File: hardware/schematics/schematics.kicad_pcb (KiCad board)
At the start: 2 copper layers, 25 parts, among them J1 Jack-DC, J2 Conn_01x20, J3 Conn_01x20, Q1 Q_NMOS_DGS, U1 ESP32-DevKitC, U2 L7805, U3 MAX6921AUI+

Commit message: Main PCB completed
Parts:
- added REF**: TestPoint_Plated_Hole_D2.0mm, TestPoint:TestPoint_Plated_Hole_D2.0mm, F.Cu at (130.8, 128.3)
- added REF**: TestPoint_Plated_Hole_D2.0mm, TestPoint:TestPoint_Plated_Hole_D2.0mm, F.Cu at (156.2, 125.7)
- added REF**: TestPoint_Plated_Hole_D2.0mm, TestPoint:TestPoint_Plated_Hole_D2.0mm, F.Cu at (92.7, 121.9)
- added REF**: MountingHole_3.2mm_M3_Pad, MountingHole:MountingHole_3.2mm_M3_Pad, F.Cu at (163.8, 137.2)
- added REF**: MountingHole_3.2mm_M3_Pad, MountingHole:MountingHole_3.2mm_M3_Pad, F.Cu at (74.9, 137.2)
- added REF**: MountingHole_3.2mm_M3_Pad, MountingHole:MountingHole_3.2mm_M3_Pad, F.Cu at (74.9, 83.8)
- added REF**: MountingHole_3.2mm_M3_Pad, MountingHole:MountingHole_3.2mm_M3_Pad, F.Cu at (163.8, 83.8)
- F1: footprint Capacitor_THT:C_Disc_D7.5mm_W4.4mm_P5.00mm -> Fuse:Fuse_Littelfuse_395Series
- J2: footprint Connector_PinHeader_2.54mm:PinHeader_2x10_P2.54mm_Vertical -> Connector_PinSocket_2.54mm:PinSocket_2x10_P2.54mm_Horizontal
- J3: footprint Connector_PinHeader_2.54mm:PinHeader_2x10_P2.54mm_Vertical -> Connector_PinSocket_2.54mm:PinSocket_2x10_P2.54mm_Vertical
- U2: footprint Package_TO_SOT_THT:TO-220-3_Vertical -> Package_TO_SOT_THT:TO-220-3_Horizontal_TabDown
- U3: footprint callisto:MAX6921AUI+ -> Package_SO:TSSOP-28_4.4x9.7mm_P0.65mm
- moved J1 149.4 mm to (152.4, 134.2), turned to 90 degrees
- moved L1 97.8 mm to (105.4, 138.4), turned to 90 degrees
- moved Q1 95.2 mm to (109.2, 128.3), turned to 180 degrees
- moved F1 72.0 mm to (144.8, 133.3), turned to 270 degrees
- moved C2 70.2 mm to (138.4, 123.2), turned to 90 degrees
- moved U2 69.5 mm to (133.3, 138.4), turned to 90 degrees
- moved C1 69.0 mm to (144.8, 123.2), turned to 90 degrees
- moved U1 63.3 mm to (143.5, 102.9), turned to 90 degrees
- moved J2 62.0 mm to (105.4, 83.8), turned to 270 degrees
- moved C4 61.6 mm to (137.2, 135.9)
- moved D4 59.9 mm to (82.5, 128.3), turned to 270 degrees
- moved D2 55.7 mm to (144.8, 128.3)
- moved D3 53.9 mm to (87.6, 128.3)
- moved D1 52.9 mm to (165.1, 120.7), turned to 180 degrees
- moved C6 49.9 mm to (88.9, 133.4), turned to 270 degrees
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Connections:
- J1 pad 3: (no net) -> GND
- J2 pad 10: /dig_3 -> /O_4
- J2 pad 11: /dig_2 -> /O_19
- J2 pad 12: /dig_1 -> /O_3
- J2 pad 13: /seg_h -> /O_18
- J2 pad 14: /seg_g -> /O_2
- J2 pad 15: /seg_f -> /O_17
- J2 pad 16: /seg_e -> /O_1
- J2 pad 17: /seg_d -> /O_16
- J2 pad 18: /seg_c -> /O_0
- J2 pad 19: /seg_b -> GND
- J2 pad 2: GND -> /O_8
- J2 pad 20: /seg_a -> GND
- J2 pad 3: /fil_v -> /O_13
- J2 pad 4: /dig_9 -> /O_7
- J2 pad 5: /dig_8 -> /O_12
- J2 pad 6: /dig_7 -> /O_6
- J2 pad 7: /dig_6 -> /O_11
- J2 pad 8: /dig_5 -> /O_5
- J2 pad 9: /dig_4 -> /O_10
- R3 pad 1: VCC -> Net-(J2-Pad1)
- R3 pad 2: /fil_v -> VCC
- U1 pad J2_11: /BLANK -> Net-(U1-PadJ2_11)
- U1 pad J2_3: Net-(U1-PadJ2_3) -> /BRIGHTNESS
- U1 pad J2_7: /BRIGHTNESS -> /PWM
- U1 pad J3_12: /PWM -> Net-(U1-PadJ3_12)
- U1 pad J3_6: Net-(U1-PadJ3_6) -> /BLANK
- U3 pad 1: /seg_e -> /O_4
- U3 pad 10: Net-(U3-Pad10) -> /O_19
- U3 pad 11: Net-(U3-Pad11) -> /O_18
- U3 pad 12: Net-(U3-Pad12) -> /O_17
- U3 pad 13: /dig_9 -> /O_16
- U3 pad 14: /dig_8 -> Net-(U3-Pad14)
- U3 pad 15: /dig_7 -> Net-(U3-Pad15)
- U3 pad 16: /dig_6 -> /O_13
- U3 pad 17: /dig_5 -> /O_12
- U3 pad 18: /dig_4 -> /O_11
- U3 pad 19: /dig_3 -> /O_10
- U3 pad 2: /seg_d -> /O_3
- U3 pad 24: /dig_2 -> Net-(U3-Pad24)
- U3 pad 25: /dig_1 -> /O_8
- U3 pad 26: /seg_h -> /O_7
- U3 pad 27: /seg_g -> /O_6
- U3 pad 28: /seg_f -> /O_5
- U3 pad 3: /seg_c -> /O_2
- U3 pad 4: /seg_b -> /O_1
- U3 pad 5: /seg_a -> /O_0
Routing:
- net VCC: track 0.00 -> 110.9 mm, vias 0 -> 2
- net +9V: track 0.00 -> 87.2 mm
- net /DIN: track 0.00 -> 63.8 mm
- net /LOAD: track 0.00 -> 61.9 mm, vias 0 -> 2
- net /CLK: track 0.00 -> 55.7 mm, vias 0 -> 2
- net /BLANK: track 0.00 -> 53.0 mm
- net VBB: track 0.00 -> 48.7 mm
- net /BRIGHTNESS: track 0.00 -> 40.0 mm, vias 0 -> 1
- net +3V3: track 0.00 -> 35.7 mm, vias 0 -> 1
- net /PWM: track 0.00 -> 30.9 mm
- net /O_13: track 0.00 -> 28.2 mm, vias 0 -> 1
- net /O_16: track 0.00 -> 28.2 mm, vias 0 -> 1
- net /O_12: track 0.00 -> 27.2 mm, vias 0 -> 1
- net /O_17: track 0.00 -> 27.2 mm, vias 0 -> 1
- net /O_11: track 0.00 -> 26.2 mm, vias 0 -> 1
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- added copper zone on B.Cu, net GND
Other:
- board outline added: 99.1 x 63.5 mm
- board text added: "9V"
- board text added: "VBB"
- board text added: "VCC"

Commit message: Tube PCB wired
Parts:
- removed the REF** at (163.8, 137.2)
- removed the REF** at (74.9, 137.2)
- removed the REF** at (74.9, 83.8)
- added REF**: MountingHole_3.2mm_M3_Pad, MountingHole:MountingHole_3.2mm_M3_Pad, F.Cu at (248.9, 148.0)
- added REF**: MountingHole_3.2mm_M3_Pad, MountingHole:MountingHole_3.2mm_M3_Pad, F.Cu at (160.0, 148.0)
- added REF**: MountingHole_3.2mm_M3_Pad, MountingHole:MountingHole_3.2mm_M3_Pad, F.Cu at (160.0, 94.6)
- J2: footprint Connector_PinSocket_2.54mm:PinSocket_2x10_P2.54mm_Horizontal -> Connector_PinSocket_2.54mm:PinSocket_2x10_P2.54mm_Vertical
- moved J3 146.4 mm to (60.3, 65.4), turned to 180 degrees
- moved DS1 122.6 mm to (93.3, 51.4), turned to 0 degrees
- moved REF** 85.8 mm to (177.8, 132.7)
- moved U3 85.8 mm to (179.1, 113.7)
- moved C1 85.8 mm to (229.9, 134.0)
- moved C2 85.8 mm to (223.5, 134.0)
- moved C3 85.8 mm to (222.2, 141.6)
- moved C4 85.8 mm to (222.2, 146.7)
- moved C5 85.8 mm to (236.2, 134.0)
- moved C6 85.8 mm to (174.0, 144.2)
- moved C7 85.8 mm to (180.3, 144.2)
- moved D1 85.8 mm to (250.2, 131.4)
- moved D2 85.8 mm to (229.9, 139.1)
- moved D3 85.8 mm to (172.7, 139.1)
- moved F1 85.8 mm to (229.9, 144.1)
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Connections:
- DS1 pad 1: GND -> /fil_g
- J1 pad 3: GND -> (no net)
- J2 pad 1: Net-(J2-Pad1) -> GND
- J2 pad 19: GND -> Net-(J2-Pad19)
- J3 pad 1: Net-(J3-Pad1) -> /dig_2
- J3 pad 10: /dig_3 -> /seg_h
- J3 pad 11: /dig_2 -> /dig_5
- J3 pad 12: /dig_1 -> /seg_a
- J3 pad 13: /seg_h -> /dig_3
- J3 pad 14: /seg_g -> /seg_f
- J3 pad 15: /seg_f -> /dig_1
- J3 pad 16: /seg_e -> /seg_b
- J3 pad 17: /seg_d -> /dig_9
- J3 pad 18: /seg_c -> /seg_g
- J3 pad 19: /seg_b -> Net-(J3-Pad19)
- J3 pad 2: GND -> /fil_g
- J3 pad 20: /seg_a -> /fil_v
- J3 pad 3: /fil_v -> /dig_4
- J3 pad 4: /dig_9 -> /seg_e
- J3 pad 5: /dig_8 -> /dig_6
- J3 pad 6: /dig_7 -> /seg_c
- J3 pad 7: /dig_6 -> /dig_7
- J3 pad 8: /dig_5 -> /seg_d
- J3 pad 9: /dig_4 -> /dig_8
- R3 pad 1: Net-(J2-Pad1) -> Net-(J2-Pad19)
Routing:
- net /seg_e: track 0.00 -> 40.0 mm
- net /seg_g: track 0.00 -> 39.5 mm
- net /seg_b: track 0.00 -> 38.0 mm
- net /seg_c: track 0.00 -> 36.8 mm
- net /seg_f: track 0.00 -> 36.8 mm
- net /seg_a: track 0.00 -> 35.1 mm
- net /seg_d: track 0.00 -> 34.7 mm
- net /dig_2: track 0.00 -> 34.1 mm
- net /fil_g: track 0.00 -> 33.0 mm
- net /seg_h: track 0.00 -> 33.0 mm
- net /dig_4: track 0.00 -> 32.0 mm
- net /dig_9: track 0.00 -> 32.0 mm
- net /fil_v: track 0.00 -> 30.9 mm
- net Net-(J2-Pad19): track 0.00 -> 30.5 mm
- net /dig_6: track 0.00 -> 30.4 mm
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
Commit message: Tube PCB created
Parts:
- moved J3 105.3 mm to (164.5, 81.3)
- moved DS1 92.7 mm to (184.8, 66.6)
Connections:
- J3 pad 19: Net-(J3-Pad19) -> (no net)
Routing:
- net /fil_v: track 30.9 -> 17.9 mm
- net /dig_9: track 32.0 -> 19.0 mm
- net /dig_1: track 29.9 -> 17.0 mm
- net /seg_h: track 33.0 -> 20.1 mm
- net /seg_d: track 34.7 -> 22.0 mm
- net /seg_c: track 36.8 -> 24.4 mm
- net /dig_4: track 32.0 -> 19.6 mm
- net /seg_e: track 40.0 -> 27.6 mm
- net /dig_6: track 30.4 -> 18.0 mm
- net /dig_8: track 28.7 -> 16.3 mm
- net /dig_7: track 29.3 -> 16.9 mm
- net /dig_5: track 28.6 -> 16.1 mm
- net /dig_3: track 28.9 -> 16.4 mm
- net /dig_2: track 34.1 -> 21.7 mm
- net /fil_g: track 33.0 -> 20.6 mm
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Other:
- board size 99.1 x 63.5 mm -> 99.2 x 96.4 mm

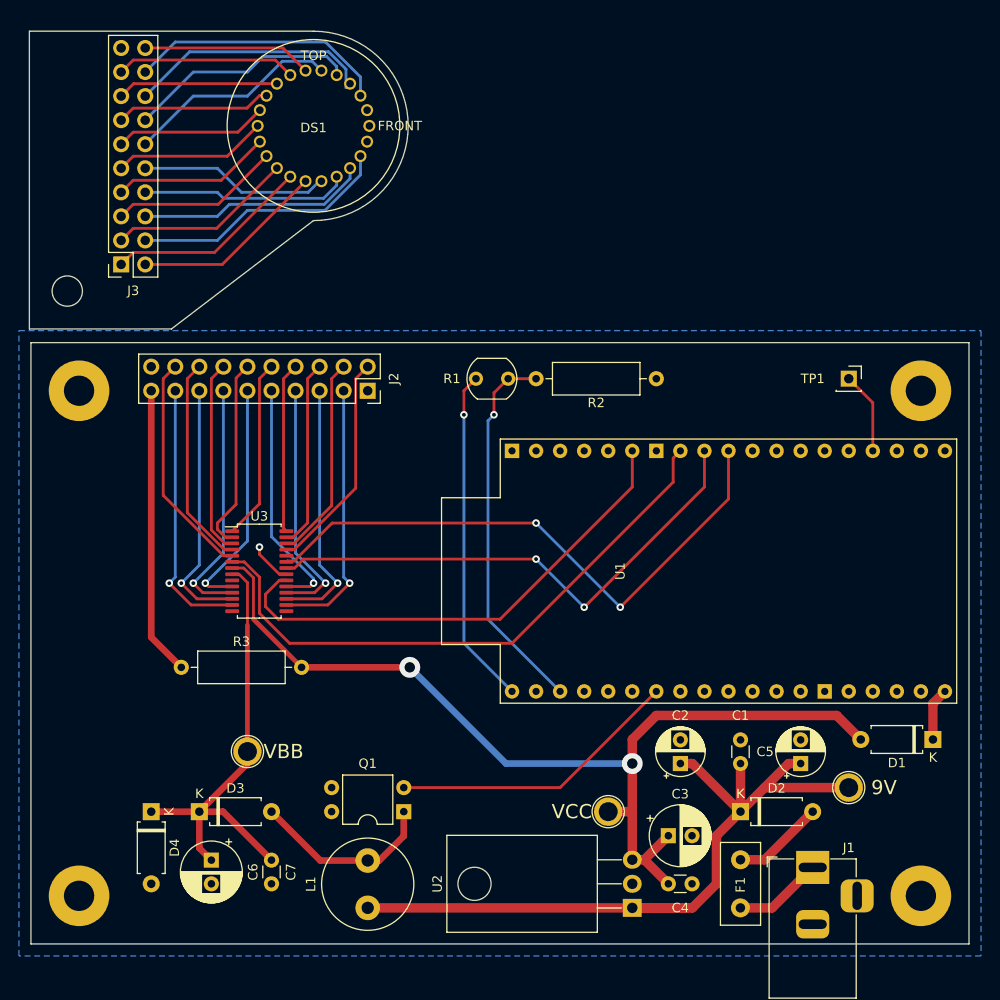
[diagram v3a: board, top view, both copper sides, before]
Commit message: Capacitor placements tweaked
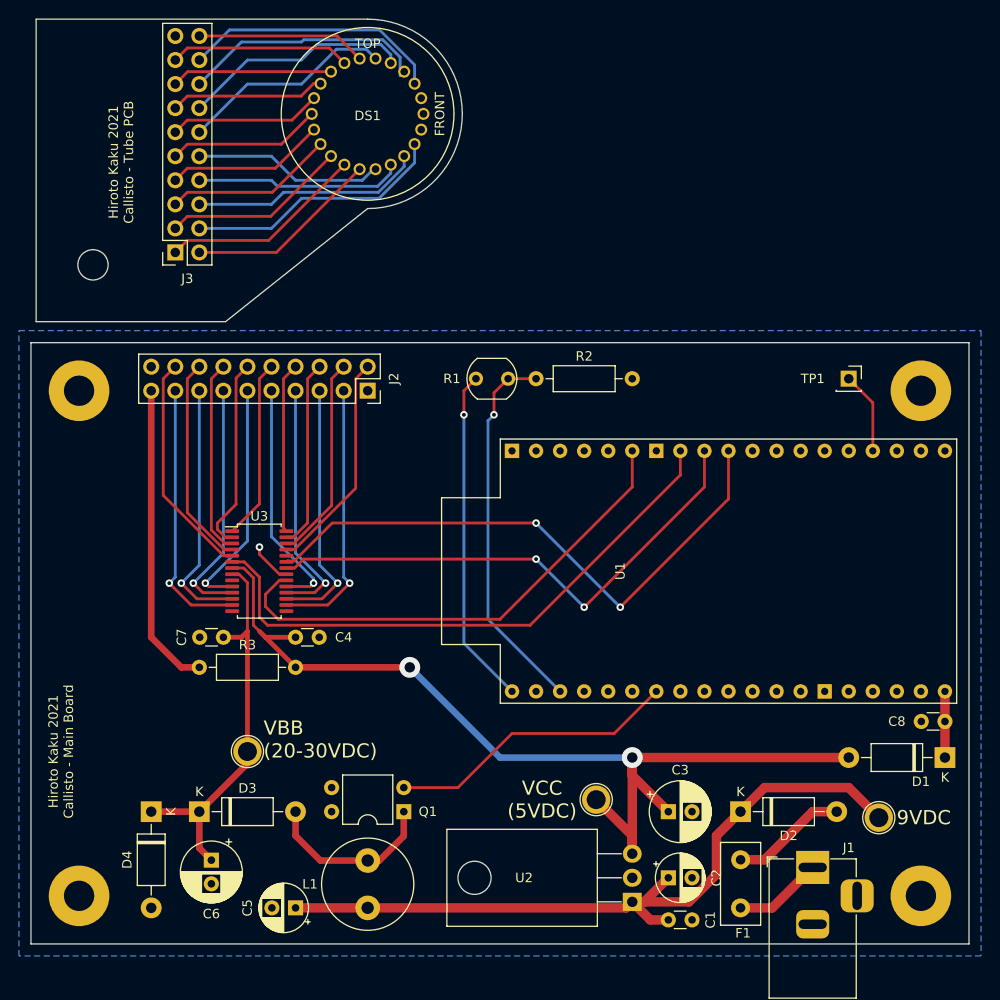
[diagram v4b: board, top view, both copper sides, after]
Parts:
- added C8: 0.1U/50V, Capacitor_THT:C_Disc_D3.0mm_W1.6mm_P2.50mm, F.Cu at (251.5, 129.5)
- C1, C4: value 0.1U -> 0.1U/50V
- C2: value 10U/25V -> 47U/25V
- C3: value 220U/6V -> 220U/6.3V
- C6: value 33U/100V -> 22U/100V
- D1, D2, D3, D4: footprint Diode_THT:D_A-405_P7.62mm_Horizontal -> Diode_THT:D_DO-41_SOD81_P10.16mm_Horizontal
- L1: value 2220U -> 2220H
- Q1: value Q_NMOS_DGS -> IRLD110PBF
- R2, R3: footprint Resistor_THT:R_Axial_DIN0309_L9.0mm_D3.2mm_P12.70mm_Horizontal -> Resistor_THT:R_Axial_DIN0207_L6.3mm_D2.5mm_P10.16mm_Horizontal
- moved C5 55.5 mm to (182.9, 149.2), turned to 180 degrees
- moved C4 47.2 mm to (182.9, 120.7)
- moved C7 24.1 mm to (175.3, 120.7), turned to 180 degrees
- moved C1 18.2 mm to (222.2, 150.5), turned to 0 degrees
- moved C2 12.1 mm to (222.2, 146.1), turned to 0 degrees
- moved DS1 5.85 mm to (190.5, 65.4)
- moved J3 5.85 mm to (170.2, 80.0)
- moved REF** 4.49 mm to (244.5, 139.7)
- moved C3 2.54 mm to (222.2, 139.1)
- moved D1 2.29 mm to (251.5, 133.3)
- moved R3 1.91 mm to (172.7, 123.8)
- moved REF** 1.80 mm to (214.6, 137.8)
- moved U2 0.63 mm to (218.4, 148.6)
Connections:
- J3 pad 19: (no net) -> Net-(J3-Pad19)
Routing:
- net +9V: track 87.2 -> 79.8 mm
- net VBB: track 48.7 -> 41.8 mm
- net Net-(D2-Pad2): track 9.72 -> 12.3 mm
- net Net-(J2-Pad19): track 30.5 -> 32.4 mm
- net Net-(C8-Pad1): track 5.61 -> 6.98 mm
- net /DIN: track 63.8 -> 62.4 mm
- net Net-(D3-Pad2): track 19.8 -> 18.7 mm
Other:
- board size 99.2 x 96.4 mm -> 99.1 x 97.7 mm
- board text added: "9VDC"
- board text added: "Hiroto Kaku 2021 Callisto - Main Board"
- board text added: "Hiroto Kaku 2021 Callisto - Tube PCB"
- board text added: "VBB (20-30VDC)"
- board text added: "VCC (5VDC)"
- board text removed: "9V"
- board text removed: "VBB"
- board text removed: "VCC"

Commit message: PCB finalized
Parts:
- added REF**: MountingHole_3.2mm_M3_Pad, MountingHole:MountingHole_3.2mm_M3_Pad, F.Cu at (161.5, 81.3)
- C1, C4, C8: value 0.1U/50V -> 0.1U/50V
- D4: value D_Zener -> 1N5262B
- R1: footprint OptoDevice:R_LDR_5.1x4.3mm_P3.4mm_Vertical -> Connector_PinHeader_2.54mm:PinHeader_1x02_P2.54mm_Vertical
- TP1: footprint Connector_PinSocket_2.54mm:PinSocket_1x01_P2.54mm_Vertical -> Connector_PinHeader_2.54mm:PinHeader_1x01_P2.54mm_Vertical
- U2: footprint Package_TO_SOT_THT:TO-220-3_Horizontal_TabDown -> Package_TO_SOT_THT:TO-220-3_Vertical
- moved C3 20.5 mm to (202.6, 144.8), turned to 270 degrees
- moved C5 12.3 mm to (194.3, 144.8), turned to 270 degrees
- moved C1 7.01 mm to (221.6, 143.5)
- moved Q1 5.72 mm to (188.6, 139.1), turned to 90 degrees
- moved U2 5.43 mm to (216.5, 143.5), turned to 180 degrees
- moved L1 4.96 mm to (186.7, 146.1), turned to 180 degrees
- moved REF** 3.70 mm to (211.5, 135.9), turned to 90 degrees
- moved R1 1.27 mm to (200.7, 93.3), turned to 90 degrees
- moved C2 0.90 mm to (222.9, 146.7), turned to 270 degrees
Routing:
- net +9V: track 79.8 -> 87.2 mm
- net Net-(D3-Pad2): track 18.7 -> 13.2 mm
- net /PWM: track 30.9 -> 35.1 mm
- net VCC: track 103.0 -> 105.0 mm, vias 2 -> 0
- net /BRIGHTNESS: track 40.0 -> 41.3 mm
- net +3V3: track 35.7 -> 35.1 mm
- added copper zone on B.Cu, net /fil_g
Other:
- outline, holes or cut-outs redrawn
